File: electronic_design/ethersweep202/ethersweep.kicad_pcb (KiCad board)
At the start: 2 copper layers, 79 x 38 mm, 73 parts, among them J1 AVR-ISP-6, J2 Conn_01x02_Male, J3 Conn_01x04_Female, J4 Conn_01x02_Male, J5 Conn_01x02_Male, J6 HR911105A, J7 Conn_01x06_Female, J8 AVR-ISP-6, J9 Conn_01x06_Male, M1 Stepper_Motor_bipolar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

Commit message: minor v202 changes
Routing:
- net SDA: track 78.2 -> 77.6 mm

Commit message: reversed xt60 polarity
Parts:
- added C24: C100nF, Capacitor_SMD:C_0805_2012Metric, F.Cu at (263.8, 77.2)
- added C25: C100nF, Capacitor_SMD:C_0805_2012Metric, F.Cu at (246.3, 98.8)
- added C26: C100nF, Capacitor_SMD:C_0805_2012Metric, F.Cu at (263.8, 80.2)
- added C27: C100nF, Capacitor_SMD:C_0805_2012Metric, F.Cu at (257.6, 87.5)
- added C28: C100nF, Capacitor_SMD:C_0805_2012Metric, F.Cu at (263.8, 83.2)
- added C29: C100nF, Capacitor_SMD:C_0805_2012Metric, F.Cu at (250.7, 98.8)
- added C30: C10uF, Capacitor_SMD:C_0805_2012Metric, F.Cu at (257.6, 90.5)
- added C31: C1uF, Capacitor_SMD:C_0805_2012Metric, F.Cu at (262.1, 87.5)
- added C32: C1uF, Capacitor_SMD:C_0805_2012Metric, F.Cu at (257.6, 93.5)
- added J10: HR911105A, modules:HANRUN_HR911105A, F.Cu at (234.3, 87.4)
- added R19: R330, Resistor_SMD:R_0603_1608Metric, F.Cu at (255.0, 98.6)
- added R20: R330, Resistor_SMD:R_0603_1608Metric, F.Cu at (261.9, 90.2)
- added U6: W5500, Package_QFP:LQFP-48_7x7mm_P0.5mm, F.Cu at (249.7, 91.6)
- C4, C5: value C22pF -> C18pF
- moved J2 15.2 mm to (190.3, 127.6), turned to 180 degrees
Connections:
- J2 pad 1: +12V -> GND
- J2 pad 2: GND -> +12V

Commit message: layout refresh
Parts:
- moved J2 13.2 mm to (189.7, 114.4)
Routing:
- net GND: vias 191 -> 190
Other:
- outline, holes or cut-outs redrawn

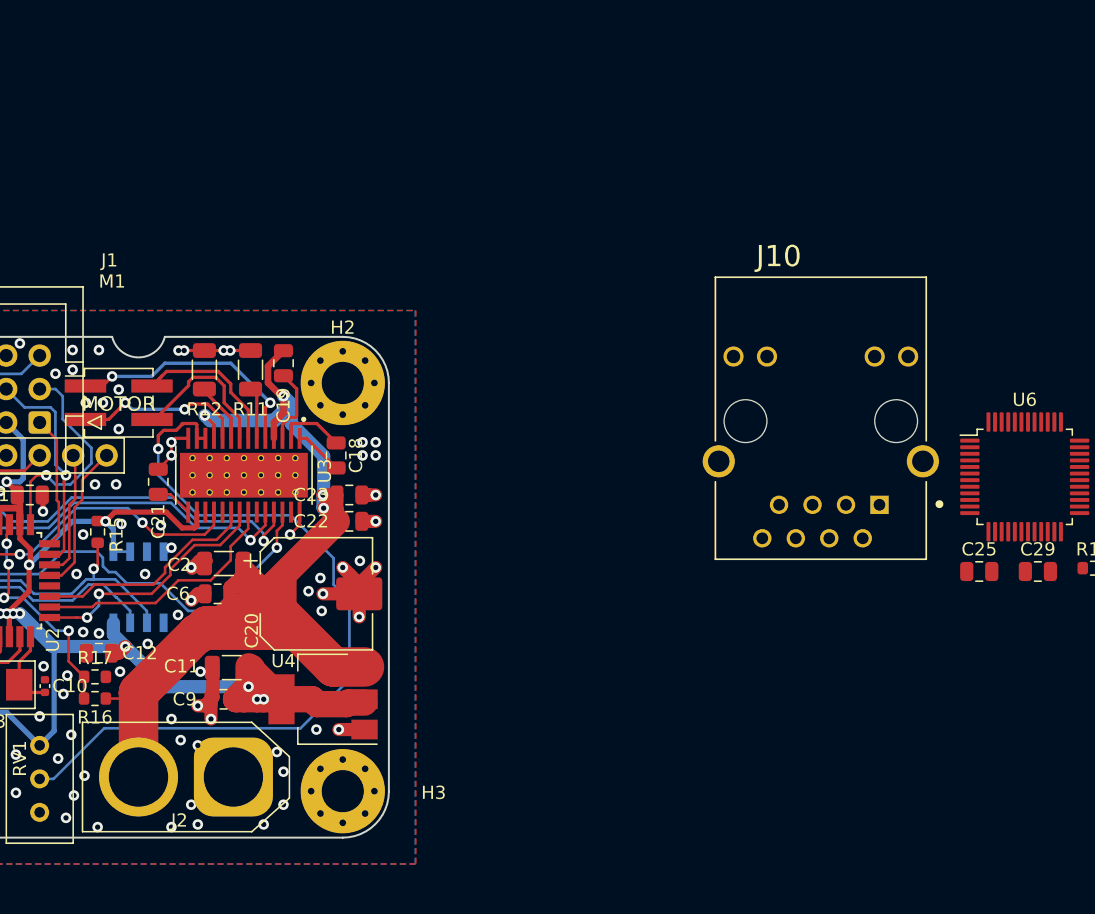
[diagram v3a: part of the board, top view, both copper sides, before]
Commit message: 202 design changed to w5500 ethernet driver
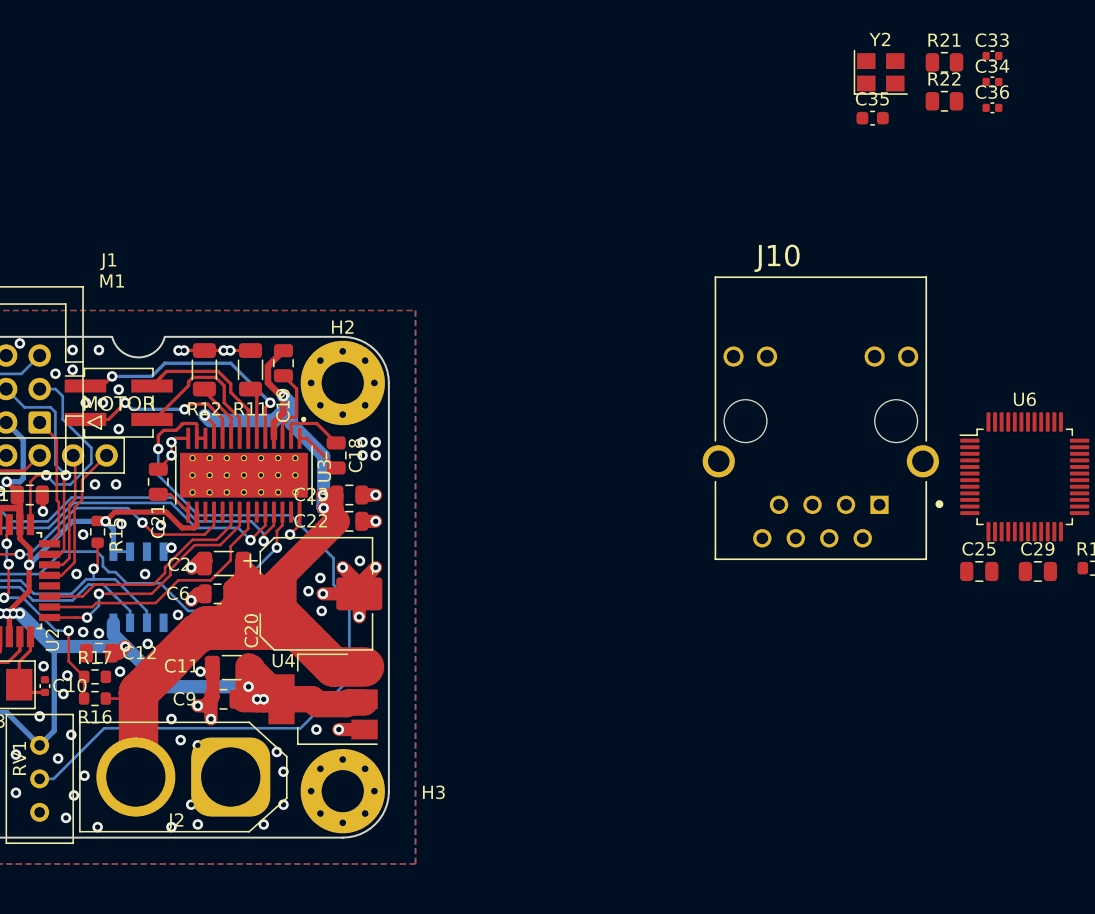
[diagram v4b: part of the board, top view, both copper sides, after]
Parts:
- added C33: C18pF, Capacitor_SMD:C_0402_1005Metric, F.Cu at (247.3, 59.7)
- added C34: C18pF, Capacitor_SMD:C_0402_1005Metric, F.Cu at (247.3, 61.7)
- added C35: C10nF, Capacitor_SMD:C_0603_1608Metric, F.Cu at (238.2, 64.4)
- added C36: C4.7uF, Capacitor_SMD:C_0402_1005Metric, F.Cu at (247.3, 63.6)
- added R21: R1M, Resistor_SMD:R_0805_2012Metric, F.Cu at (243.7, 60.2)
- added R22: R12K4, Resistor_SMD:R_0805_2012Metric, F.Cu at (243.7, 63.1)
- added Y2: Crystal_25MHz, Crystal:Crystal_SMD_3225-4Pin_3.2x2.5mm, F.Cu at (238.8, 60.9)
- moved J2 0.20 mm to (189.5, 114.4)
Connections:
- net FLT_ETHERNET renamed FLT_STEPPER
- net Net-(U6-Pad36) renamed ETH_INT
- net Net-(U6-Pad37) renamed ETH_RST
- J10 pad 15: GND -> GND1
- J10 pad 16: GND -> GND1
- J10 pad 8: GND -> GND1
- U3 pad 17: Net-(U3-Pad17) -> +3V3
- U6 pad 14: Net-(U6-Pad14) -> GND
- U6 pad 16: Net-(U6-Pad14) -> GND
- U6 pad 19: Net-(U6-Pad14) -> GND
- U6 pad 29: Net-(U6-Pad29) -> GND
- U6 pad 3: Net-(U6-Pad14) -> GND
- U6 pad 43: Net-(U6-Pad43) -> +3V3
- U6 pad 44: Net-(U6-Pad44) -> +3V3
- U6 pad 45: Net-(U6-Pad45) -> +3V3
- U6 pad 48: Net-(U6-Pad14) -> GND
- U6 pad 9: Net-(U6-Pad14) -> GND
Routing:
- net +3V3: track 226.5 -> 224.5 mm

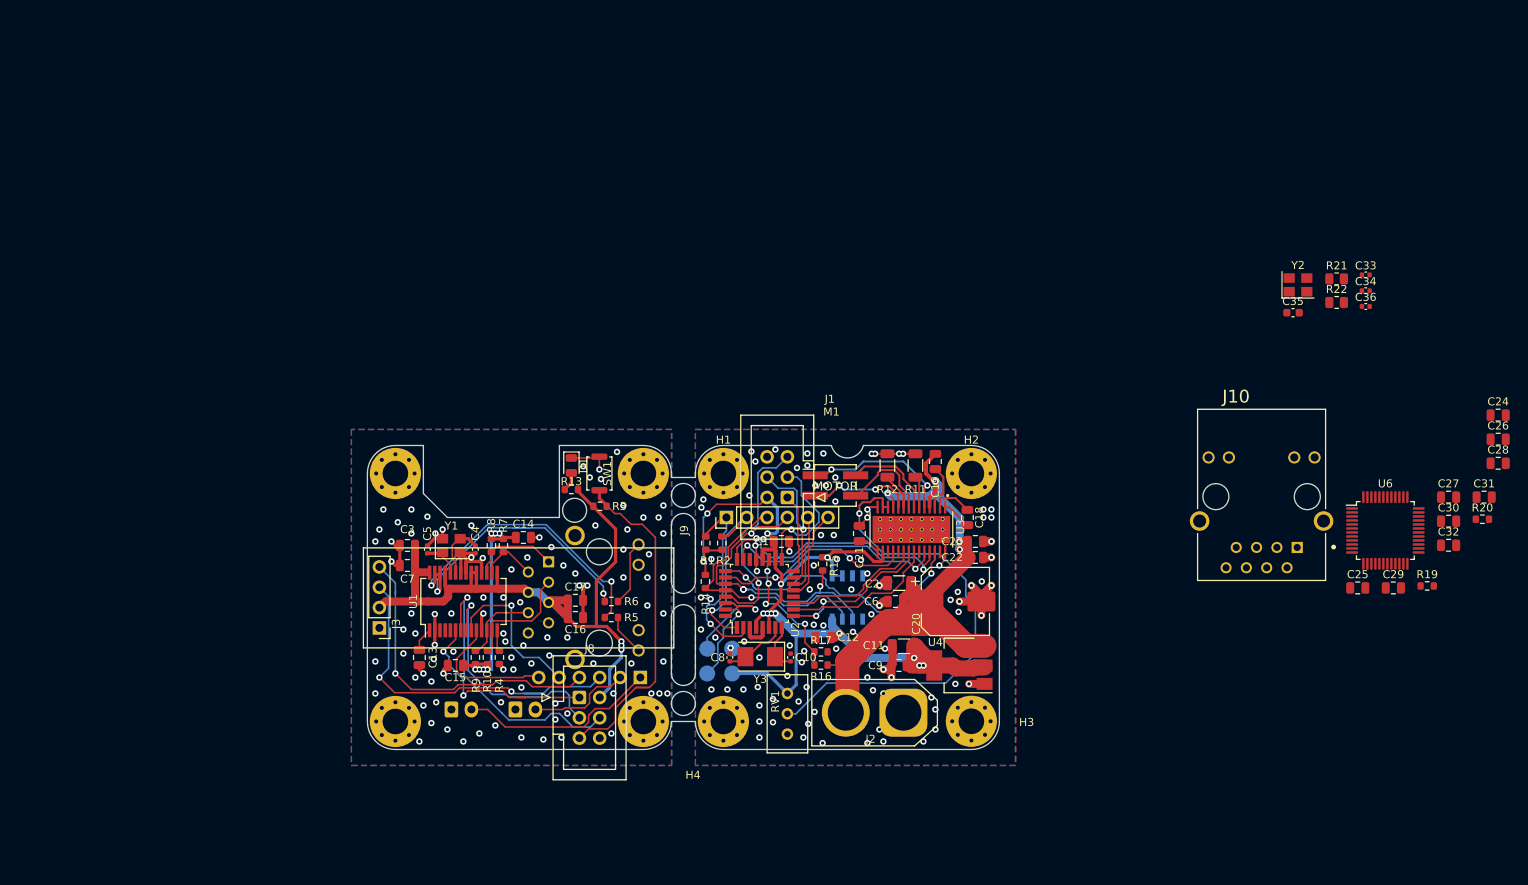
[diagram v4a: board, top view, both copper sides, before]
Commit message: layout implementation board 1 done, board 2 in progress
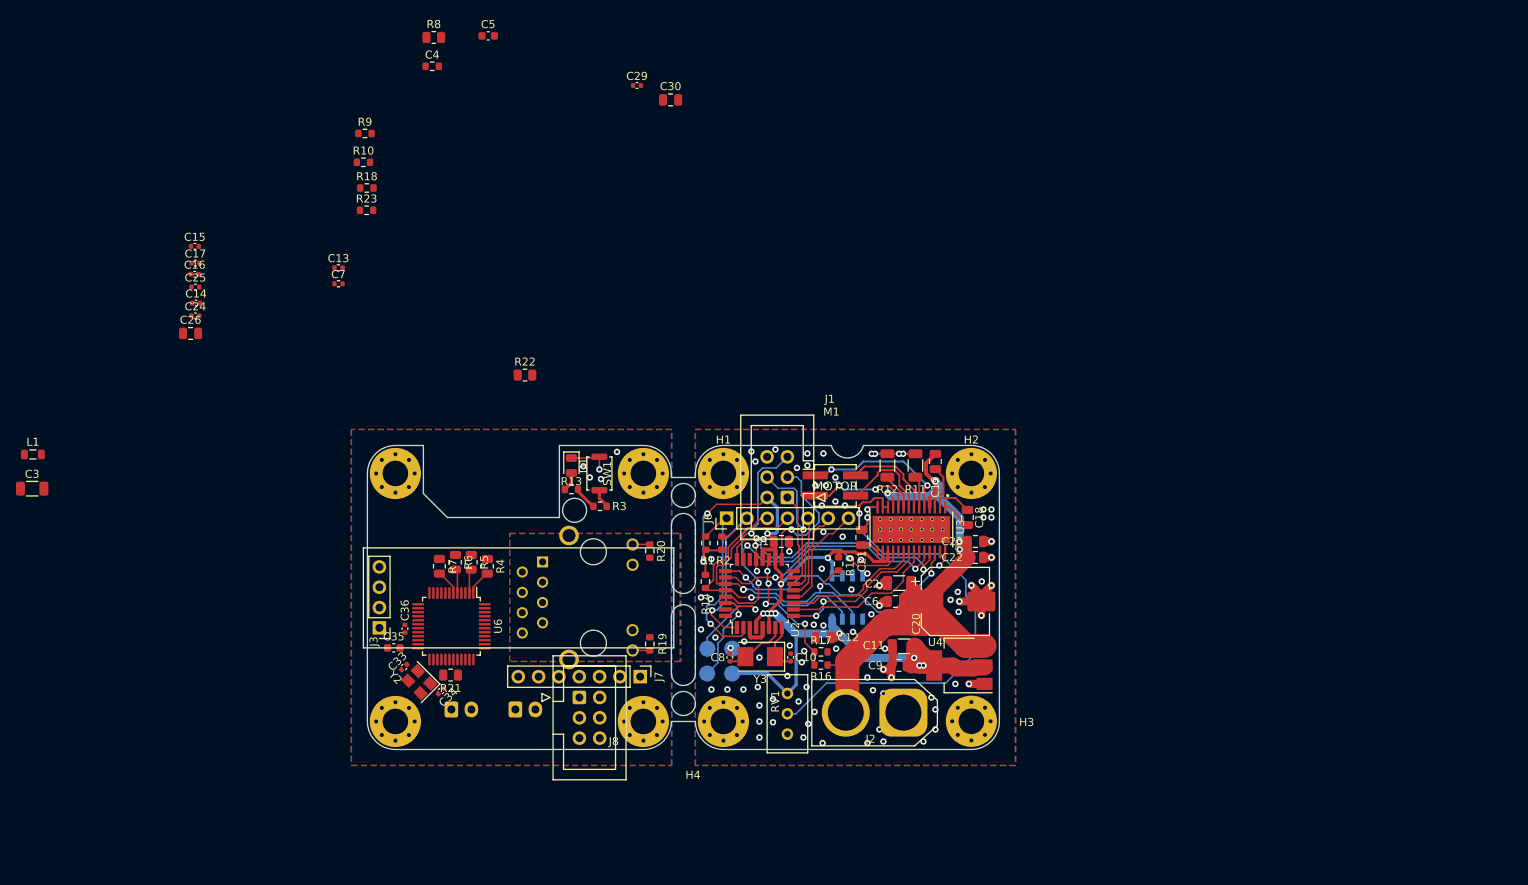
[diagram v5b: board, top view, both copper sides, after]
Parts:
- removed C27, C28: C100nF, Capacitor_SMD:C_0805_2012Metric
- removed C31, C32: C1uF, Capacitor_SMD:C_0805_2012Metric
- removed J9: Conn_01x06_Male, Connector_PinHeader_2.54mm:PinHeader_1x06_P2.54mm_Vertical
- removed U1: ENC28J60x-SS, Package_SO:SSOP-28_5.3x10.2mm_P0.65mm
- removed Y1: Crystal_25MHz, Crystal:Crystal_SMD_3225-4Pin_3.2x2.5mm
- added L1: L600OHM, Inductor_SMD:L_0805_2012Metric, F.Cu at (80.7, 82.1)
- added R18: R49.9, Resistor_SMD:R_0603_1608Metric, F.Cu at (122.4, 48.8)
- added R23: R49.9, Resistor_SMD:R_0603_1608Metric, F.Cu at (122.4, 51.6)
- C13, C7: value C1uF -> C6.8nF; footprint Capacitor_SMD:C_0805_2012Metric -> Resistor_SMD:R_0402_1005Metric
- C14, C15, C16, C17: value C1uF -> C100nF; footprint Capacitor_SMD:C_0805_2012Metric -> Capacitor_SMD:C_0402_1005Metric
- C24, C25, C29: footprint Capacitor_SMD:C_0805_2012Metric -> Capacitor_SMD:C_0402_1005Metric
- C26: value C100nF -> C10uF
- C3: value C1uF -> C1nF; footprint Capacitor_SMD:C_0805_2012Metric -> Resistor_SMD:R_1206_3216Metric
- C4: value C18pF -> C22nF; footprint Capacitor_SMD:C_0402_1005Metric -> Resistor_SMD:R_0603_1608Metric
- C5: value C18pF -> C10nF; footprint Capacitor_SMD:C_0402_1005Metric -> Capacitor_SMD:C_0603_1608Metric
- J10: moved to B.Cu
- J6: value HR911105A -> Conn_01x07_Female; footprint modules:HANRUN_HR911105A -> Connector_PinHeader_2.54mm:PinHeader_1x07_P2.54mm_Vertical; moved to F.Cu
- J7: value Conn_01x06_Female -> Conn_01x07_Male; footprint Connector_PinHeader_2.54mm:PinHeader_1x06_P2.54mm_Vertical -> Connector_PinHeader_2.54mm:PinHeader_1x07_P2.54mm_Vertical; moved to F.Cu
- R10, R9: value R1k -> R49.9
- R4, R7: value R1k -> R33; footprint Resistor_SMD:R_0603_1608Metric -> Resistor_SMD:R_0805_2012Metric
- R5, R6: value R330 -> R33; footprint Resistor_SMD:R_0603_1608Metric -> Resistor_SMD:R_0805_2012Metric
- R8: value R1k -> R10; footprint Resistor_SMD:R_0603_1608Metric -> Resistor_SMD:R_0805_2012Metric
- moved C26 164.0 mm to (100.4, 67.0)
- moved C24 163.3 mm to (101.0, 64.8)
- moved C25 150.1 mm to (101.0, 61.2)
- moved C33 129.8 mm to (127.1, 108.7), turned to 225 degrees
- moved C36 126.7 mm to (127.2, 103.9), turned to 90 degrees
- moved C34 126.0 mm to (131.7, 111.7), turned to 225 degrees
- moved R21 121.3 mm to (132.9, 109.7), turned to 180 degrees
- moved Y2 120.5 mm to (129.0, 110.6), turned to 135 degrees
- moved C35 120.0 mm to (125.8, 106.3), turned to 180 degrees
- moved U6 117.4 mm to (133.0, 103.6), turned to 270 degrees
- moved C29 113.5 mm to (156.2, 36.0)
- moved C30 110.6 mm to (160.4, 37.8)
- moved R20 104.2 mm to (157.8, 94.2), turned to 270 degrees
- moved R22 101.9 mm to (142.2, 72.2)
- moved R19 97.4 mm to (157.8, 105.8), turned to 90 degrees
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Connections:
- C13 pad 1: Net-(C13-Pad1) -> RD+
- C13 pad 2: GND -> Net-(C13-Pad2)
- C14 pad 1: Net-(C14-Pad1) -> +3.3VA
- C15 pad 1: Net-(C14-Pad1) -> +3.3VA
- C16 pad 1: +3V3 -> +3.3VA
- C17 pad 1: +3V3 -> +3.3VA
- C24 pad 1: +3V3 -> +3.3VA
- C25 pad 1: +3V3 -> +3.3VA
- C26 pad 1: +3V3 -> +3.3VA
- C3 pad 1: +3V3 -> GND1
- C4 pad 2: Net-(C4-Pad2) -> TC
- C5 pad 1: Net-(C5-Pad1) -> GND
- C5 pad 2: GND -> RC
- C7 pad 1: +3V3 -> RD-
- C7 pad 2: GND -> Net-(C7-Pad2)
- J10 pad 1: ENC_TD+ -> TD+
- J10 pad 2: ENC_TD- -> TD-
- J10 pad 3: ENC_RD+ -> RD+
- J10 pad 4: +3V3 -> TC
- J10 pad 5: +3V3 -> RC
- J10 pad 6: ENC_RD- -> RD-
- J6 pad 1: ENC_TD+ -> ESTOP
- J6 pad 2: ENC_TD- -> ENDSTOP
- J6 pad 3: ENC_RD+ -> SCL
- J6 pad 4: +3V3 -> SDA
- J6 pad 5: +3V3 -> CS_ETHERNET
- J6 pad 6: ENC_RD- -> RST_ETHERNET
- J6 pad 7: (no net) -> ETH_INT
- R10 pad 1: Net-(C14-Pad1) -> +3.3VA
- R10 pad 2: ENC_RD+ -> TD+
- R4 pad 1: GND -> TD-
- R5 pad 1: ETHERNET_LED_A -> TD+
- R6 pad 1: ETHERNET_LED_B -> Net-(C7-Pad2)
- R7 pad 1: Net-(C14-Pad1) -> Net-(C13-Pad2)
- R7 pad 2: ENC_TD- -> Net-(R7-Pad2)
- R8 pad 1: Net-(C14-Pad1) -> +3.3VA
- R8 pad 2: ENC_TD+ -> TC
- R9 pad 1: Net-(C14-Pad1) -> +3.3VA
- R9 pad 2: ENC_RD- -> TD-
- U2 pad 12: Net-(U2-Pad12) -> ETH_INT
- U6 pad 1: Net-(U6-Pad1) -> Net-(R4-Pad2)
- U6 pad 2: Net-(U6-Pad2) -> Net-(R5-Pad2)
- U6 pad 37: ETH_RST -> RST_ETHERNET
- U6 pad 5: Net-(U6-Pad5) -> Net-(R6-Pad2)
- U6 pad 6: Net-(U6-Pad6) -> Net-(R7-Pad2)
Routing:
- net +3V3: track 224.5 -> 136.2 mm, vias 16 -> 13
- net SCL: track 77.7 -> 33.3 mm, vias 3 -> 1
- net rst: track 70.0 -> 29.4 mm
- net GND: track 92.1 -> 51.7 mm, vias 190 -> 98
- net SDA: track 77.6 -> 39.1 mm, vias 5 -> 4
- net MOSI: track 52.5 -> 17.4 mm, vias 2 -> 1
- net Net-(R5-Pad2): track 35.6 -> 3.02 mm, vias 2 -> 0
- net Net-(C14-Pad1): track 32.4 -> 0.00 mm, vias 7 -> 0
- net Net-(R6-Pad2): track 34.5 -> 3.03 mm, vias 2 -> 0
- net SCK: track 47.1 -> 17.6 mm, vias 2 -> 1
- net MISO: track 36.3 -> 10.1 mm, vias 2 -> 0
- net ESTOP: track 50.3 -> 25.3 mm
- net CS_ETHERNET: track 29.6 -> 9.85 mm, vias 1 -> 0
- net RST_ETHERNET: track 28.3 -> 11.7 mm
- net ENC_RD+: track 14.6 -> 0.00 mm
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- added copper zone on B.Cu, net GND1
- added copper zone on F.Cu, net GND1
